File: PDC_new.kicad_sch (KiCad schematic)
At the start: 83 parts, among them J1 Conn_01x02_Pin, J10 Conn_01x02_Pin, J11 XT90PW(2+2)-M.G.Y, J12 Conn_01x02_Pin, J13 QS8, J14 Conn_01x02_Pin, J15 Conn_01x02_Pin, J2 Conn_01x02_Pin, J3 Conn_01x02_Pin, J4 Conn_01x02_Pin, J5 Conn_01x02_Pin, J6 Conn_01x02_Pin, J7 Conn_01x02_Pin, J8 Conn_01x02_Pin, J9 Conn_01x02_Pin, Q2 IRF540NSTRLPBF, U1 TPSI3050QDWZRQ1, U10 LM393LVDR, U11 IPB017N10N5ATMA1, U12 IPB017N10N5ATMA1, U14 IPB017N10N5ATMA1, U2 TPSI3050QDWZRQ1, U4 74HC74, U5 URB4805LD-60WR3, U6 IPB017N10N5ATMA1, U7 TLC555CDR, U8 SN74HC08D, U9 SN74HC14DR

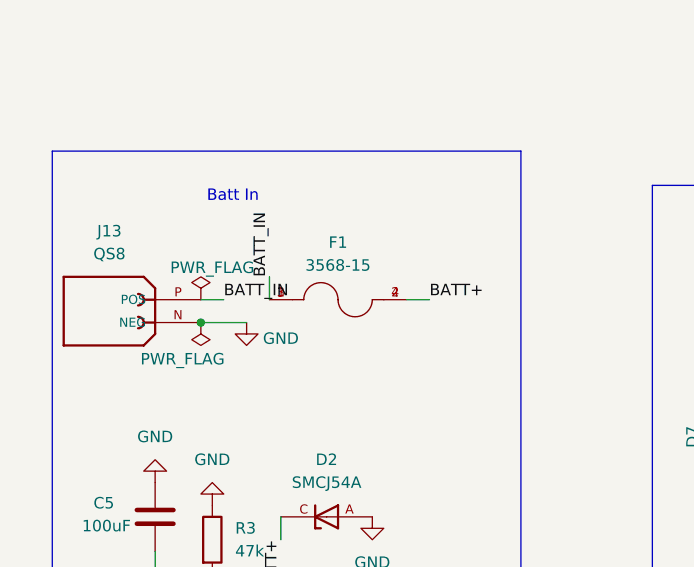
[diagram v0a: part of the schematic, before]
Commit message: updated layout
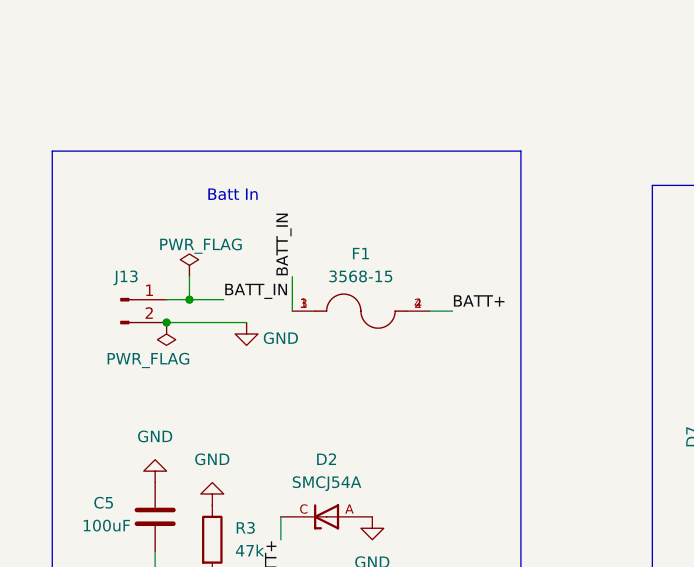
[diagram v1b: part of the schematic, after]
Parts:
- removed J13: QS8, QS8_S_Connectors:QS8-S-M_Vertical_DirectCup, symbol XT90I:XT90PW-F
- added J13: Conn_01x02_Pin, QS8_S_Connectors:QS8-S-M_Vertical_DirectCup, symbol Connector:Conn_01x02_Pin
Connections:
- net BATT_IN: now also J13.1 (Pin_1)
- net GND: now also J13.2 (Pin_2)
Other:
- moved on the sheet: F1
